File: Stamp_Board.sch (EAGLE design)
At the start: 312 parts, among them SW1 CT10-XXXX-A2, SW10 CT10-XXXX-A2, SW100 CT10-XXXX-A2, SW101 CT10-XXXX-A2, SW102 CT10-XXXX-A2, SW103 CT10-XXXX-A2, SW104 CT10-XXXX-A2, SW105 CT10-XXXX-A2, SW106 CT10-XXXX-A2, SW107 CT10-XXXX-A2, SW108 CT10-XXXX-A2, SW109 CT10-XXXX-A2, SW11 CT10-XXXX-A2, SW110 CT10-XXXX-A2, SW111 CT10-XXXX-A2, SW112 CT10-XXXX-A2, SW113 CT10-XXXX-A2, SW114 CT10-XXXX-A2, SW115 CT10-XXXX-A2, SW116 CT10-XXXX-A2, SW117 CT10-XXXX-A2, SW118 CT10-XXXX-A2, SW119 CT10-XXXX-A2, SW12 CT10-XXXX-A2, SW120 CT10-XXXX-A2, SW121 CT10-XXXX-A2, SW122 CT10-XXXX-A2, SW123 CT10-XXXX-A2, SW124 CT10-XXXX-A2, SW125 CT10-XXXX-A2, SW126 CT10-XXXX-A2, SW127 CT10-XXXX-A2, SW128 CT10-XXXX-A2, SW129 CT10-XXXX-A2, SW13 CT10-XXXX-A2, SW130 CT10-XXXX-A2, SW131 CT10-XXXX-A2, SW132 CT10-XXXX-A2, SW14 CT10-XXXX-A2, SW15 CT10-XXXX-A2, SW16 CT10-XXXX-A2, SW17 CT10-XXXX-A2, SW18 CT10-XXXX-A2, SW19 CT10-XXXX-A2, SW2 CT10-XXXX-A2, SW20 CT10-XXXX-A2, SW21 CT10-XXXX-A2, SW22 CT10-XXXX-A2, SW23 CT10-XXXX-A2, SW24 CT10-XXXX-A2, SW25 CT10-XXXX-A2, SW26 CT10-XXXX-A2, SW27 CT10-XXXX-A2, SW28 CT10-XXXX-A2, SW29 CT10-XXXX-A2, SW3 CT10-XXXX-A2, SW30 CT10-XXXX-A2, SW31 CT10-XXXX-A2, SW32 CT10-XXXX-A2, SW33 CT10-XXXX-A2, SW34 CT10-XXXX-A2, SW35 CT10-XXXX-A2, SW36 CT10-XXXX-A2, SW37 CT10-XXXX-A2, SW38 CT10-XXXX-A2, SW39 CT10-XXXX-A2, SW4 CT10-XXXX-A2, SW40 CT10-XXXX-A2, SW41 CT10-XXXX-A2, SW42 CT10-XXXX-A2, SW43 CT10-XXXX-A2, SW44 CT10-XXXX-A2, SW45 CT10-XXXX-A2, SW46 CT10-XXXX-A2, SW47 CT10-XXXX-A2, SW48 CT10-XXXX-A2, SW49 CT10-XXXX-A2, SW5 CT10-XXXX-A2, SW50 CT10-XXXX-A2, SW51 CT10-XXXX-A2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

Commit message: Adding Stamp board schematic and board layout. Updated SR name labels and updated LED array.
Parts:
- removed C8: (no value), rcl:C-USC0805
- removed LED1, LED10, LED100, LED101, LED102, LED103, LED104, LED105, LED106, LED107, LED108, LED109, LED11, LED110, LED111, LED112, LED113, LED114, LED115, LED116, LED117, LED118, LED119, LED12, LED120, LED121, LED122, LED123, LED124, LED125, LED126, LED127, LED128, LED129, LED13, LED130, LED131, LED132, LED133, LED134, LED135, LED136, LED137, LED138, LED139, LED14, LED15, LED16, LED17, LED18, LED19, LED2, LED20, LED21, LED22, LED23, LED24, LED25, LED26, LED27, LED28, LED29, LED3, LED30, LED31, LED32, LED33, LED34, LED35, LED36, LED37, LED38, LED39, LED4, LED40, LED41, LED42, LED43, LED44, LED45, LED46, LED47, LED48, LED49, LED5, LED50, LED51, LED52, LED53, LED54, LED55, LED56, LED57, LED58, LED59, LED6, LED60, LED61, LED62, LED63, LED64, LED65, LED66, LED67, LED68, LED69, LED7, LED70, LED71, LED72, LED73, LED74, LED75, LED76, LED77, LED78, LED79, LED8, LED80, LED81, LED82, LED83, LED84, LED85, LED86, LED87, LED88, LED89, LED9, LED90, LED91, LED92, LED93, LED94, LED95, LED96, LED97, LED98, LED99: (no value), led:LEDSMT1206
- removed R3: (no value), rcl:R-US_M0805
- removed SW1, SW10, SW100, SW101, SW102, SW103, SW104, SW105, SW106, SW107, SW108, SW109, SW11, SW110, SW111, SW112, SW113, SW114, SW115, SW116, SW117, SW118, SW119, SW12, SW120, SW121, SW122, SW123, SW124, SW125, SW126, SW127, SW128, SW129, SW13, SW130, SW131, SW132, SW14, SW15, SW16, SW17, SW18, SW19, SW2, SW20, SW21, SW22, SW23, SW24, SW25, SW26, SW27, SW28, SW29, SW3, SW30, SW31, SW32, SW33, SW34, SW35, SW36, SW37, SW38, SW39, SW4, SW40, SW41, SW42, SW43, SW44, SW45, SW46, SW47, SW48, SW49, SW5, SW50, SW51, SW52, SW53, SW54, SW55, SW56, SW57, SW58, SW59, SW6, SW60, SW61, SW62, SW63, SW64, SW65, SW66, SW67, SW68, SW69, SW7, SW70, SW71, SW72, SW73, SW74, SW75, SW76, SW77, SW78, SW79, SW8, SW80, SW81, SW82, SW83, SW84, SW85, SW86, SW87, SW88, SW89, SW9, SW90, SW91, SW92, SW93, SW94, SW95, SW96, SW97, SW98, SW99: CT10-XXXX-A2, switch-coto:CT10-XXXX-A2
- removed U$10, U$11, U$12, U$13, U$14, U$15, U$16, U$17, U$18, U$19, U$20, U$21, U$22, U$23, U$24, U$25, U$3, U$4, U$5, U$6, U$7, U$8, U$9: MM74HC595TSSOP-LD16, ECE477_Guitutar:MM74HC595TSSOP-LD16
- removed U$2: BM78SPP05MC2/NC2, ECE477_Guitutar:BM78SPP05MC2/NC2
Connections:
- removed net EAN: U$2.EAN
- removed net GND: LED10.C, LED100.C, LED101.C, LED102.C, LED103.C, LED104.C, LED105.C, LED106.C, LED107.C, LED108.C, LED109.C, LED11.C, LED110.C, LED111.C, LED112.C, LED113.C, LED114.C, LED115.C, LED116.C, LED117.C, LED118.C, LED119.C, LED12.C, LED120.C, LED121.C, LED122.C, LED123.C, LED124.C, LED125.C, LED126.C, LED127.C, LED128.C, LED129.C, LED13.C, LED130.C, LED131.C, LED132.C, LED133.C, LED134.C, LED135.C, LED136.C, LED137.C, LED138.C, LED139.C, LED14.C, LED15.C, LED16.C, LED17.C, LED18.C, LED19.C, LED2.C, LED20.C, LED21.C, LED22.C, LED23.C, LED24.C, LED25.C, LED26.C, LED27.C, LED28.C, LED29.C, LED3.C, LED30.C, LED31.C, LED32.C, LED33.C, LED34.C, LED35.C, LED36.C, LED37.C, LED38.C, LED39.C, LED4.C, LED40.C, LED41.C, LED42.C, LED43.C, LED44.C, LED45.C, LED46.C, LED47.C, LED48.C, LED49.C, LED5.C, LED50.C, LED51.C, LED52.C, LED53.C, LED54.C, LED55.C, LED56.C, LED57.C, LED58.C, LED59.C, LED6.C, LED60.C, LED61.C, LED62.C, LED63.C, LED64.C, LED65.C, LED66.C, LED67.C, LED68.C, LED69.C, LED7.C, LED70.C, LED71.C, LED72.C, LED73.C, LED74.C, LED75.C, LED76.C, LED77.C, LED78.C, LED79.C, LED8.C, LED80.C, LED81.C, LED82.C, LED83.C, LED84.C, LED85.C, LED86.C, LED87.C, LED88.C, LED89.C, LED9.C, LED90.C, LED91.C, LED92.C, LED93.C, LED94.C, LED95.C, LED96.C, LED97.C, LED98.C, LED99.C, U$10.GND, U$11.GND, U$12.GND, U$13.GND, U$14.GND, U$15.GND, U$16.GND, U$17.GND, U$18.GND, U$19.GND, U$20.GND, U$21.GND, U$22.GND, U$23.GND, U$24.GND, U$25.GND, U$3.GND, U$4.GND, U$5.GND, U$6.GND, U$7.GND, U$8.GND, U$9.GND
- removed net LED: LED1.C, U$2.LED1
- removed net N$107: LED34.A, U$8.QD
- removed net N$108: LED35.A, U$8.QE
- removed net N$109: LED33.A, U$8.QC
- removed net N$11: LED5.A, U$3.QE
- removed net N$110: LED32.A, U$8.QB
- removed net N$111: LED36.A, U$8.QF
- removed net N$117: LED37.A, U$8.QA
- removed net N$118: LED40.A, U$9.QD
- removed net N$119: LED41.A, U$9.QE
- removed net N$120: LED39.A, U$9.QC
- removed net N$121: LED38.A, U$9.QB
- removed net N$122: LED42.A, U$9.QF
- removed net N$128: LED43.A, U$9.QA
- removed net N$129: LED46.A, U$10.QD
- removed net N$130: LED47.A, U$10.QE
- removed net N$131: LED45.A, U$10.QC
- removed net N$132: LED44.A, U$10.QB
- removed net N$133: LED48.A, U$10.QF
- removed net N$139: LED49.A, U$10.QA
- removed net N$140: LED52.A, U$11.QD
- removed net N$141: LED53.A, U$11.QE
- removed net N$142: LED51.A, U$11.QC
- removed net N$143: LED50.A, U$11.QB
- removed net N$144: LED54.A, U$11.QF
- removed net N$15: LED1.A, R3.1
- removed net N$150: LED55.A, U$11.QA
- removed net N$151: LED58.A, U$12.QD
- removed net N$152: LED59.A, U$12.QE
- removed net N$153: LED57.A, U$12.QC
- removed net N$154: LED56.A, U$12.QB
- removed net N$155: LED60.A, U$12.QF
- removed net N$16: R3.2, U$2.LDO33_O, U$2.VDD_IO
- removed net N$161: LED61.A, U$12.QA
- removed net N$162: LED64.A, U$13.QD
- removed net N$163: LED65.A, U$13.QE
- removed net N$164: LED63.A, U$13.QC
- removed net N$165: LED62.A, U$13.QB
- removed net N$166: LED66.A, U$13.QF
- removed net N$17: LED3.A, U$3.QC
- removed net N$172: LED67.A, U$13.QA
- removed net N$173: LED70.A, U$14.QD
- removed net N$174: LED71.A, U$14.QE
- removed net N$175: LED69.A, U$14.QC
- removed net N$176: LED68.A, U$14.QB
- removed net N$177: LED72.A, U$14.QF
- removed net N$18: LED2.A, U$3.QB
- removed net N$183: LED73.A, U$14.QA
- removed net N$184: LED76.A, U$15.QD
- removed net N$185: LED77.A, U$15.QE
- removed net N$186: LED75.A, U$15.QC
- removed net N$187: LED74.A, U$15.QB
- removed net N$188: LED78.A, U$15.QF
- removed net N$19: LED6.A, U$3.QF
- removed net N$194: LED79.A, U$15.QA
- removed net N$195: LED82.A, U$16.QD
- removed net N$196: LED83.A, U$16.QE
- removed net N$197: LED81.A, U$16.QC
- removed net N$198: LED80.A, U$16.QB
- removed net N$199: LED84.A, U$16.QF
- removed net N$205: LED85.A, U$16.QA
- removed net N$206: LED88.A, U$17.QD
- removed net N$207: LED89.A, U$17.QE
- removed net N$208: LED87.A, U$17.QC
- removed net N$209: LED86.A, U$17.QB
- removed net N$210: LED90.A, U$17.QF
- removed net N$216: LED91.A, U$17.QA
- removed net N$217: LED94.A, U$18.QD
- removed net N$218: LED95.A, U$18.QE
- removed net N$219: LED93.A, U$18.QC
- removed net N$220: LED92.A, U$18.QB
- removed net N$221: LED96.A, U$18.QF
- removed net N$227: LED97.A, U$18.QA
- removed net N$228: LED100.A, U$19.QD
- removed net N$229: LED101.A, U$19.QE
- removed net N$230: LED99.A, U$19.QC
- removed net N$231: LED98.A, U$19.QB
- removed net N$232: LED102.A, U$19.QF
- removed net N$238: LED103.A, U$19.QA
- removed net N$239: LED106.A, U$20.QD
- removed net N$240: LED107.A, U$20.QE
- removed net N$241: LED105.A, U$20.QC
- removed net N$242: LED104.A, U$20.QB
- removed net N$243: LED108.A, U$20.QF
- removed net N$249: LED109.A, U$20.QA
- removed net N$250: LED112.A, U$21.QD
- removed net N$251: LED113.A, U$21.QE
- removed net N$252: LED111.A, U$21.QC
- removed net N$253: LED110.A, U$21.QB
- removed net N$254: LED114.A, U$21.QF
- removed net N$26: LED10.A, U$4.QD
- removed net N$260: LED115.A, U$21.QA
- removed net N$261: LED118.A, U$22.QD
- removed net N$262: LED119.A, U$22.QE
- removed net N$263: LED117.A, U$22.QC
- removed net N$264: LED116.A, U$22.QB
- removed net N$265: LED120.A, U$22.QF
- removed net N$27: LED11.A, U$4.QE
- removed net N$271: LED121.A, U$22.QA
- removed net N$272: LED124.A, U$23.QD
- removed net N$273: LED125.A, U$23.QE
- removed net N$274: LED123.A, U$23.QC
- removed net N$275: LED122.A, U$23.QB
- removed net N$276: LED126.A, U$23.QF
- removed net N$28: LED9.A, U$4.QC
- removed net N$282: LED127.A, U$23.QA
- removed net N$283: LED130.A, U$24.QD
- removed net N$284: LED131.A, U$24.QE
- removed net N$285: LED129.A, U$24.QC
- removed net N$286: LED128.A, U$24.QB
- removed net N$287: LED132.A, U$24.QF
- removed net N$29: LED8.A, U$4.QB
- removed net N$293: LED133.A, U$24.QA
- removed net N$294: LED136.A, U$25.QD
- removed net N$295: LED137.A, U$25.QE
- removed net N$296: LED135.A, U$25.QC
- removed net N$297: LED134.A, U$25.QB
- removed net N$298: LED138.A, U$25.QF
- removed net N$30: LED12.A, U$4.QF
- removed net N$304: LED139.A, U$25.QA
- removed net N$36: LED13.A, U$4.QA
- removed net N$37: LED16.A, U$5.QD
- removed net N$38: LED17.A, U$5.QE
- removed net N$39: LED15.A, U$5.QC
- removed net N$40: LED14.A, U$5.QB
- removed net N$41: LED18.A, U$5.QF
- removed net N$54: LED19.A, U$5.QA
- removed net N$55: LED22.A, U$6.QD
- removed net N$56: LED23.A, U$6.QE
- removed net N$57: LED21.A, U$6.QC
- removed net N$58: LED20.A, U$6.QB
- removed net N$59: LED24.A, U$6.QF
- removed net N$6: LED7.A, U$3.QA
- removed net N$65: LED25.A, U$6.QA
- removed net N$69: LED28.A, U$7.QD
- removed net N$70: LED29.A, U$7.QE
- removed net N$71: LED27.A, U$7.QC
- removed net N$72: LED26.A, U$7.QB
- removed net N$73: LED30.A, U$7.QF
- removed net N$79: LED31.A, U$7.QA
- removed net N$8: LED4.A, U$3.QD
- removed net P1_2: U$2.P1_2/SCL
- removed net P1_3: U$2.P1_3/SDA
- removed net P2_0: U$2.P2_0
- removed net P2_4: U$2.P2_4
- removed net P3_6: U$2.P3_6
- removed net VCC: U$10.VCC, U$11.VCC, U$12.VCC, U$13.VCC, U$14.VCC, U$15.VCC, U$16.VCC, U$17.VCC, U$18.VCC, U$19.VCC, U$20.VCC, U$21.VCC, U$22.VCC, U$23.VCC, U$24.VCC, U$25.VCC, U$3.VCC, U$4.VCC, U$5.VCC, U$6.VCC, U$7.VCC, U$8.VCC, U$9.VCC
- net FRET1: no longer SW1.2, SW2.2, SW3.2, SW4.2, SW5.2, SW6.2
- net FRET10: no longer SW55.2, SW56.2, SW57.2, SW58.2, SW59.2, SW60.2
- net FRET11: no longer SW61.2, SW62.2, SW63.2, SW64.2, SW65.2, SW66.2
- net FRET12: no longer SW67.2, SW68.2, SW69.2, SW70.2, SW71.2, SW72.2
- net FRET13: no longer SW73.2, SW74.2, SW75.2, SW76.2, SW77.2, SW78.2
- net FRET14: no longer SW79.2, SW80.2, SW81.2, SW82.2, SW83.2, SW84.2
- net FRET15: no longer SW85.2, SW86.2, SW87.2, SW88.2, SW89.2, SW90.2
- net FRET16: no longer SW91.2, SW92.2, SW93.2, SW94.2, SW95.2, SW96.2
- net FRET17: no longer SW100.2, SW101.2, SW102.2, SW97.2, SW98.2, SW99.2
- net FRET18: no longer SW103.2, SW104.2, SW105.2, SW106.2, SW107.2, SW108.2
- net FRET19: no longer SW109.2, SW110.2, SW111.2, SW112.2, SW113.2, SW114.2
- net FRET2: no longer SW10.2, SW11.2, SW12.2, SW7.2, SW8.2, SW9.2
- net FRET20: no longer SW115.2, SW116.2, SW117.2, SW118.2, SW119.2, SW120.2
- net FRET21: no longer SW121.2, SW122.2, SW123.2, SW124.2, SW125.2, SW126.2
- net FRET22: no longer SW127.2, SW128.2, SW129.2, SW130.2, SW131.2, SW132.2
- net FRET3: no longer SW13.2, SW14.2, SW15.2, SW16.2, SW17.2, SW18.2
- net FRET4: no longer SW19.2, SW20.2, SW21.2, SW22.2, SW23.2, SW24.2
- net FRET5: no longer SW25.2, SW26.2, SW27.2, SW28.2, SW29.2, SW30.2
- net FRET6: no longer SW31.2, SW32.2, SW33.2, SW34.2, SW35.2, SW36.2
- net FRET7: no longer SW37.2, SW38.2, SW39.2, SW40.2, SW41.2, SW42.2
- net FRET8: no longer SW43.2, SW44.2, SW45.2, SW46.2, SW47.2, SW48.2
- net FRET9: no longer SW49.2, SW50.2, SW51.2, SW52.2, SW53.2, SW54.2
- net G: no longer U$10.G, U$11.G, U$12.G, U$13.G, U$14.G, U$15.G, U$16.G, U$17.G, U$18.G, U$19.G, U$20.G, U$21.G, U$22.G, U$23.G, U$24.G, U$25.G, U$3.G, U$4.G, U$5.G, U$6.G, U$7.G, U$8.G, U$9.G
- net LED_SER1: no longer U$3.SER
- net LED_SER10: no longer U$12.SER
- net LED_SER11: no longer U$13.SER
- net LED_SER12: no longer U$14.SER
- net LED_SER13: no longer U$15.SER
- net LED_SER14: no longer U$16.SER
- net LED_SER15: no longer U$17.SER
- net LED_SER16: no longer U$18.SER
- net LED_SER17: no longer U$19.SER
- net LED_SER18: no longer U$20.SER
- net LED_SER19: no longer U$21.SER
- net LED_SER2: no longer U$4.SER
- net LED_SER20: no longer U$22.SER
- net LED_SER21: no longer U$23.SER
- net LED_SER22: no longer U$24.SER
- net LED_SER23: no longer U$25.SER
- net LED_SER3: no longer U$5.SER
- net LED_SER4: no longer U$6.SER
- net LED_SER5: no longer U$7.SER
- net LED_SER6: no longer U$8.SER
- net LED_SER7: no longer U$9.SER
- net LED_SER8: no longer U$10.SER
- net LED_SER9: no longer U$11.SER
- net P0_0: no longer U$2.P0_0
- net P0_4: no longer U$2.P0_4
- net P0_5: no longer U$2.P0_5
- net P1_5: no longer U$2.P1_5
- net P1_7: no longer U$2.P1_7
- net P3_1: no longer U$2.P3_1
- net P3_2: no longer U$2.P3_2
- net P3_3: no longer U$2.P3_3
- net P3_4: no longer U$2.P3_4
- net P3_7: no longer U$2.P3_7
- net PE: no longer C8.2, U$2.GND, U$2.GND1
- net RCK: no longer U$10.RCK, U$11.RCK, U$12.RCK, U$13.RCK, U$14.RCK, U$15.RCK, U$16.RCK, U$17.RCK, U$18.RCK, U$19.RCK, U$20.RCK, U$21.RCK, U$22.RCK, U$23.RCK, U$24.RCK, U$25.RCK, U$3.RCK, U$4.RCK, U$5.RCK, U$6.RCK, U$7.RCK, U$8.RCK, U$9.RCK
- net RST_N: no longer U$2.RST_N
- net RXD: no longer U$2.HCI_RXD
- net SCK: no longer U$10.SCK, U$11.SCK, U$12.SCK, U$13.SCK, U$14.SCK, U$15.SCK, U$16.SCK, U$17.SCK, U$18.SCK, U$19.SCK, U$20.SCK, U$21.SCK, U$22.SCK, U$23.SCK, U$24.SCK, U$25.SCK, U$3.SCK, U$4.SCK, U$5.SCK, U$6.SCK, U$7.SCK, U$8.SCK, U$9.SCK
- net SCLR: no longer U$10.SCLR, U$11.SCLR, U$12.SCLR, U$13.SCLR, U$14.SCLR, U$15.SCLR, U$16.SCLR, U$17.SCLR, U$18.SCLR, U$19.SCLR, U$20.SCLR, U$21.SCLR, U$22.SCLR, U$23.SCLR, U$24.SCLR, U$25.SCLR, U$3.SCLR, U$4.SCLR, U$5.SCLR, U$6.SCLR, U$7.SCLR, U$8.SCLR, U$9.SCLR
- net STRING1: no longer SW1.1, SW102.1, SW108.1, SW114.1, SW12.1, SW120.1, SW126.1, SW132.1, SW18.1, SW24.1, SW30.1, SW36.1, SW42.1, SW48.1, SW54.1, SW60.1, SW66.1, SW72.1, SW78.1, SW84.1, SW90.1, SW96.1
- net STRING2: no longer SW103.1, SW109.1, SW115.1, SW121.1, SW127.1, SW13.1, SW19.1, SW2.1, SW25.1, SW31.1, SW37.1, SW43.1, SW49.1, SW55.1, SW61.1, SW67.1, SW7.1, SW73.1, SW79.1, SW85.1, SW91.1, SW97.1
- net STRING3: no longer SW104.1, SW110.1, SW116.1, SW122.1, SW128.1, SW14.1, SW20.1, SW26.1, SW3.1, SW32.1, SW38.1, SW44.1, SW50.1, SW56.1, SW62.1, SW68.1, SW74.1, SW8.1, SW80.1, SW86.1, SW92.1, SW98.1
- net STRING4: no longer SW105.1, SW111.1, SW117.1, SW123.1, SW129.1, SW15.1, SW21.1, SW27.1, SW33.1, SW39.1, SW4.1, SW45.1, SW51.1, SW57.1, SW63.1, SW69.1, SW75.1, SW81.1, SW87.1, SW9.1, SW93.1, SW99.1
- net STRING5: no longer SW10.1, SW100.1, SW106.1, SW112.1, SW118.1, SW124.1, SW130.1, SW16.1, SW22.1, SW28.1, SW34.1, SW40.1, SW46.1, SW5.1, SW52.1, SW58.1, SW64.1, SW70.1, SW76.1, SW82.1, SW88.1, SW94.1
- net STRING6: no longer SW101.1, SW107.1, SW11.1, SW113.1, SW119.1, SW125.1, SW131.1, SW17.1, SW23.1, SW29.1, SW35.1, SW41.1, SW47.1, SW53.1, SW59.1, SW6.1, SW65.1, SW71.1, SW77.1, SW83.1, SW89.1, SW95.1
- net SW_BTN: no longer U$2.SW_BTN
- net TXD: no longer U$2.HCI_TXD
- net VDD: no longer C8.1, U$2.BAT_IN
- net WAKEUP: no longer U$2.WAKEUP

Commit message: Added oscillator schematic to Stamp Board and started layout corrections.
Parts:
- added C8, C9: (no value), rcl:C-USC0805
- added R3, R4: (no value), rcl:R-US_M0805
- added Y1: (no value), SparkFun-Clocks:CRYSTALSMD-5X3.2-2PAD
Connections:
- removed net N$10: C6.1, JP4.11, U$1.VDD5
- removed net N$42: JP2.1, U$1.PGEC2/AN6/RPB6/RB6
- removed net N$43: JP2.2, U$1.PGED2/AN7/RPB7/CTED3/RB7
- removed net N$7: C4.1, JP2.21, U$1.VDD3
- removed net N$9: C5.2, JP3.12, JP3.5, U$1.VDD4, U$1.VUSB3V3
- new net GND: C8.1, C9.1
- new net N$11: JP3.14, R3.1, U$1.OSC2/CLKO/RC15
- new net N$15: JP3.13, R4.1, U$1.OSC1/CLKI/RC12
- new net N$6: C8.2, R3.2, Y1.2
- new net N$8: C9.2, R4.2, Y1.1
- net FRET16: now also JP2.1, U$1.PGEC2/AN6/RPB6/RB6; no longer JP3.13, U$1.OSC1/CLKI/RC12
- net FRET17: now also JP2.2, U$1.PGED2/AN7/RPB7/CTED3/RB7; no longer JP3.14, U$1.OSC2/CLKO/RC15
- net VDD: now also C4.1, C5.2, C6.1, JP2.21, JP3.12, JP3.5, JP4.11, U$1.VDD3, U$1.VDD4, U$1.VDD5, U$1.VUSB3V3
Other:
- moved on the sheet: C1, C2, C3, C4, C5, C6, C7, ICSP, JP1, JP2, JP3, JP4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

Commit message: Completed stamp board layout
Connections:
- net P0_0 renamed P2_0
- removed net PE: C1.2, C7.1
- net GND: now also C1.2, C7.1
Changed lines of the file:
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@@
 <?xml version="1.0" encoding="utf-8"?>
 <!DOCTYPE eagle SYSTEM "eagle.dtd">
-<eagle version="8.0.0">
+<eagle version="8.0.1">
 <drawing>
 <settings>
@@
 <part name="R1" library="rcl" deviceset="R-US_" device="M0805"/>
 <part name="R2" library="rcl" deviceset="R-US_" device="M0805"/>
-<part name="PE4" library="supply1" deviceset="PE" device=""/>
-<part name="PE5" library="supply1" deviceset="PE" device=""/>
+<part name="GND" library="supply1" deviceset="PE" device="" value="GND"/>
+<part name="GND2" library="supply1" deviceset="PE" device="" value="GND"/>
 <part name="JP1" library="pinhead" deviceset="PINHD-1X25" device=""/>
 <part name="JP2" library="pinhead" deviceset="PINHD-1X25" device=""/>
@@
 <instance part="R1" gate="G$1" x="93.98" y="154.94"/>
 <instance part="R2" gate="G$1" x="86.36" y="162.56" rot="R90"/>
-<instance part="PE4" gate="M" x="86.36" y="142.24"/>
-<instance part="PE5" gate="M" x="215.9" y="243.84" rot="R180"/>
+<instance part="GND" gate="M" x="86.36" y="139.7"/>
+<instance part="GND2" gate="M" x="215.9" y="246.38" rot="R180"/>
 <instance part="JP1" gate="A" x="139.7" y="154.94"/>
 <instance part="JP2" gate="A" x="208.28" y="86.36" rot="R90"/>
@@
 </segment>
 </net>
-<net name="PE" class="0">
-<segment>
-<pinref part="C1" gate="G$1" pin="2"/>
-<pinref part="PE4" gate="M" pin="PE"/>
-</segment>
-<segment>
-<pinref part="C7" gate="G$1" pin="1"/>
-<pinref part="PE5" gate="M" pin="PE"/>
-</segment>
-</net>
 <net name="P1_5" class="0">
 <segment>
@@
 </segment>
 </net>
-<net name="P0_0" class="0">
+<net name="P2_0" class="0">
 <segment>
 <pinref part="U$1" gate="G$1" pin="AN19/C2INC/RPG9/PMA2/RG9"/>
 <pinref part="JP1" gate="A" pin="14"/>
 <wire x1="142.24" y1="152.4" x2="137.16" y2="152.4" width="0.1524" layer="91"/>
-<wire x1="137.16" y1="152.4" x2="124.46" y2="152.4" width="0.1524" layer="91"/>
-<label x="124.46" y="152.4" size="1.27" layer="95" rot="R180" xref="yes"/>
+<wire x1="137.16" y1="152.4" x2="121.92" y2="152.4" width="0.1524" layer="91"/>
 <junction x="137.16" y="152.4"/>
+<label x="119.38" y="165.1" size="1.778" layer="95" rot="R90"/>
+<label x="121.92" y="152.4" size="1.27" layer="95" rot="R180" xref="yes"/>
 </segment>
 <segment>
@@
 <wire x1="322.58" y1="170.18" x2="330.2" y2="170.18" width="0.1524" layer="91"/>
 <wire x1="330.2" y1="170.18" x2="330.2" y2="162.56" width="0.1524" layer="91"/>
+<junction x="330.2" y="162.56"/>
 </segment>
 </net>
@@
 <wire x1="322.58" y1="144.78" x2="330.2" y2="144.78" width="0.1524" layer="91"/>
 <wire x1="330.2" y1="144.78" x2="330.2" y2="149.86" width="0.1524" layer="91"/>
+<junction x="330.2" y="149.86"/>
 </segment>
 </net>
@@
 <pinref part="GND1" gate="1" pin="GND"/>
 </segment>
-</net>
+<segment>
+<pinref part="C1" gate="G$1" pin="2"/>
+<pinref part="GND" gate="M" pin="PE"/>
+<wire x1="86.36" y1="142.24" x2="86.36" y2="144.78" width="0.1524" layer="91"/>
+</segment>
+<segment>
+<pinref part="C7" gate="G$1" pin="1"/>
+<pinref part="GND2" gate="M" pin="PE"/>
+<wire x1="215.9" y1="243.84" x2="215.9" y2="241.3" width="0.1524" layer="91"/>
+</segment>
+</net>

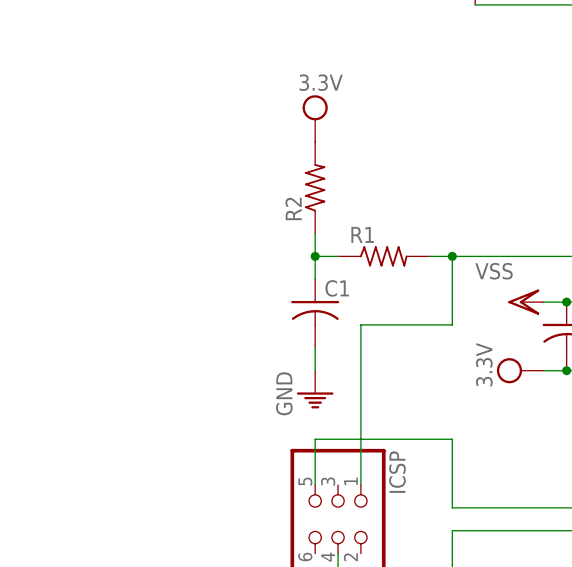
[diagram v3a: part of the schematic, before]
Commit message: Completed traces to other PCBs
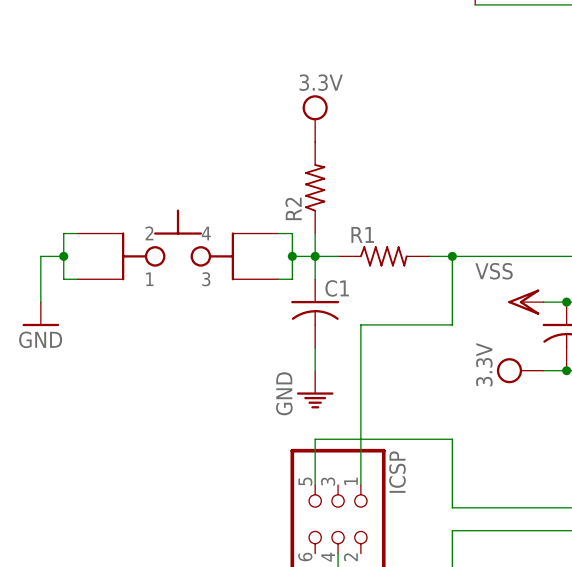
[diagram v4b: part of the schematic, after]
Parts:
- added U$2: LL3301NF065QG, ECE477_Guitutar:LL3301NF065QG
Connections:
- removed net N$1: C1.1, R1.1, R2.1
- new net N$16: C1.1, R1.1, R2.1, U$2.3, U$2.4
- net GND: now also U$2.1, U$2.2
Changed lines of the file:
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@@
 <?xml version="1.0" encoding="utf-8"?>
 <!DOCTYPE eagle SYSTEM "eagle.dtd">
-<eagle version="8.0.1">
+<eagle version="8.0.0">
 <drawing>
 <settings>
@@
 <part name="SUPPLY6" library="supply2" deviceset="VDD" device="" value="3.3V"/>
 <part name="SUPPLY7" library="supply2" deviceset="VDD" device="" value="3.3V"/>
+<part name="U$2" library="ECE477_Guitutar" deviceset="LL3301NF065QG" device=""/>
+<part name="GND3" library="supply1" deviceset="GND" device=""/>
 </parts>
 <sheets>
@@
 <instance part="SUPPLY6" gate="G$1" x="182.88" y="50.8" rot="R180"/>
 <instance part="SUPPLY7" gate="G$1" x="307.34" y="152.4" rot="R270"/>
+<instance part="U$2" gate="G$1" x="71.12" y="154.94"/>
+<instance part="GND3" gate="1" x="55.88" y="147.32"/>
 </instances>
 <busses>
 </busses>
 <nets>
-<net name="N$1" class="0">
-<segment>
-<wire x1="86.36" y1="152.4" x2="86.36" y2="154.94" width="0.1524" layer="91"/>
-<wire x1="86.36" y1="154.94" x2="86.36" y2="157.48" width="0.1524" layer="91"/>
-<wire x1="88.9" y1="154.94" x2="86.36" y2="154.94" width="0.1524" layer="91"/>
-<junction x="86.36" y="154.94"/>
-<pinref part="C1" gate="G$1" pin="1"/>
-<pinref part="R1" gate="G$1" pin="1"/>
-<pinref part="R2" gate="G$1" pin="1"/>
-</segment>
-</net>
 <net name="N$12" class="0">
 <segment>
@@
 <wire x1="215.9" y1="243.84" x2="215.9" y2="241.3" width="0.1524" layer="91"/>
 </segment>
-</net>
+<segment>
+<wire x1="58.42" y1="157.48" x2="58.42" y2="154.94" width="0.1524" layer="91"/>
+<wire x1="58.42" y1="154.94" x2="58.42" y2="152.4" width="0.1524" layer="91"/>
+<wire x1="58.42" y1="154.94" x2="55.88" y2="154.94" width="0.1524" layer="91"/>
+<wire x1="55.88" y1="154.94" x2="55.88" y2="149.86" width="0.1524" layer="91"/>
+<junction x="58.42" y="154.94"/>
+<pinref part="GND3" gate="1" pin="GND"/>
+<pinref part="U$2" gate="G$1" pin="2"/>
+<wire x1="58.42" y1="157.48" x2="59.944" y2="157.48" width="0.1524" layer="91"/>
+<pinref part="U$2" gate="G$1" pin="1"/>
+<wire x1="58.42" y1="152.4" x2="59.944" y2="152.4" width="0.1524" layer="91"/>
+</segment>
+</net>
+<net name="N$16" class="0">
+<segment>
+<wire x1="83.82" y1="157.48" x2="83.82" y2="154.94" width="0.1524" layer="91"/>
+<wire x1="83.82" y1="154.94" x2="83.82" y2="152.4" width="0.1524" layer="91"/>
+<wire x1="86.36" y1="152.4" x2="86.36" y2="154.94" width="0.1524" layer="91"/>
+<wire x1="86.36" y1="154.94" x2="86.36" y2="157.48" width="0.1524" layer="91"/>
+<wire x1="88.9" y1="154.94" x2="86.36" y2="154.94" width="0.1524" layer="91"/>
+<junction x="86.36" y="154.94"/>
+<pinref part="C1" gate="G$1" pin="1"/>
+<pinref part="R1" gate="G$1" pin="1"/>
+<pinref part="R2" gate="G$1" pin="1"/>
+<wire x1="83.82" y1="154.94" x2="86.36" y2="154.94" width="0.1524" layer="91"/>
+<junction x="83.82" y="154.94"/>
+<pinref part="U$2" gate="G$1" pin="4"/>
+<wire x1="83.82" y1="157.48" x2="82.296" y2="157.48" width="0.1524" layer="91"/>
+<pinref part="U$2" gate="G$1" pin="3"/>
+<wire x1="83.82" y1="152.4" x2="82.296" y2="152.4" width="0.1524" layer="91"/>
+</segment>
+</net>
